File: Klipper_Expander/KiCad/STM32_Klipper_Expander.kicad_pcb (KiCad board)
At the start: 2 copper layers, 100 x 24 mm, 47 parts, among them J1 USB_B_Micro, J10 Conn_01x01, J11 Conn_01x03, J12 Conn_01x02, J2 Conn_01x04, J4 Conn_01x03, J5 Vin, J6 Screw_Terminal_01x08, J7 Conn_01x02, J8 Conn_01x02, J9 Conn_01x02, Q1 IRLML6344TRPBF, Q2 IRLML6344TRPBF, Q3 IRLML6344TRPBF, Q4 IRLML6344TRPBF, SW2 SW_SPST, U1 STM32F042F6Px, U2 AP2127K-3.3, U3 74LVC1G17

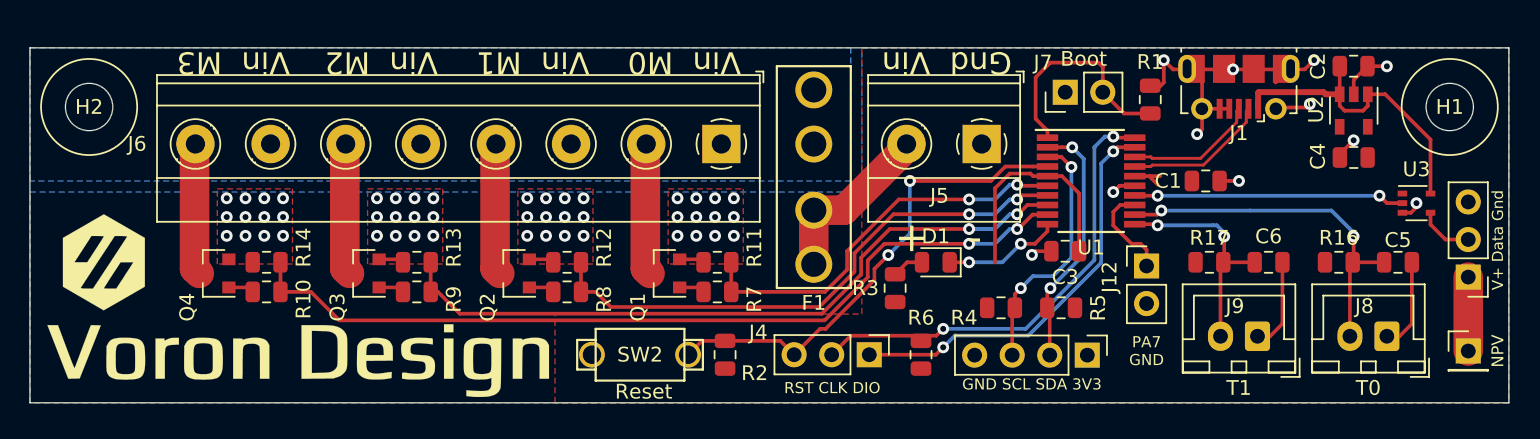
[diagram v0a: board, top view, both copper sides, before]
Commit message: Status LED's and silkscren adjustments.
Added status LED's for Vin (12/24V), USB (5V), and all 4 mosfets on the drain. LED's will signal mosfet output status.

Gerber and PNP files still need to be completed.
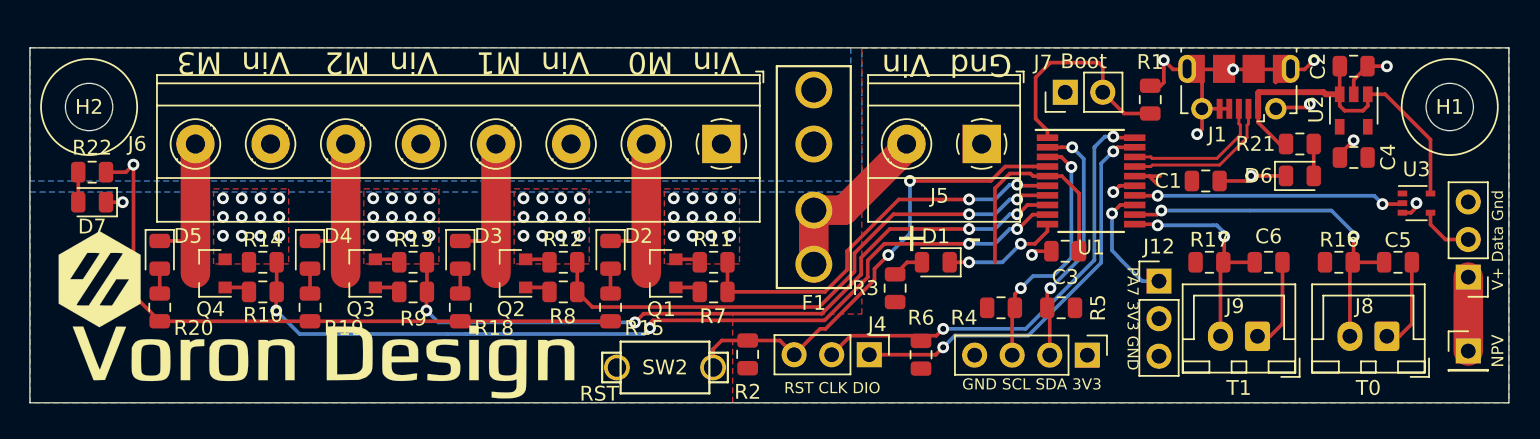
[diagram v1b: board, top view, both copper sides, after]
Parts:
- added D2: LED, LED_SMD:LED_0805_2012Metric, F.Cu at (139.3, 90.0)
- added D3: LED, LED_SMD:LED_0805_2012Metric, F.Cu at (129.1, 90.0)
- added D4: LED, LED_SMD:LED_0805_2012Metric, F.Cu at (118.9, 90.0)
- added D5: LED, LED_SMD:LED_0805_2012Metric, F.Cu at (108.8, 90.0)
- added D6: LED, LED_SMD:LED_0805_2012Metric, F.Cu at (185.9, 84.7)
- added D7: LED, LED_SMD:LED_0805_2012Metric, F.Cu at (104.2, 86.4)
- added R15: 4.7K, Resistor_SMD:R_0805_2012Metric, F.Cu at (139.3, 93.5)
- added R18: 4.7K, Resistor_SMD:R_0805_2012Metric, F.Cu at (129.1, 93.5)
- added R19: 4.7K, Resistor_SMD:R_0805_2012Metric, F.Cu at (118.9, 93.5)
- added R20: 4.7K, Resistor_SMD:R_0805_2012Metric, F.Cu at (108.8, 93.5)
- added R21: 1K, Resistor_SMD:R_0805_2012Metric, F.Cu at (185.9, 82.5)
- added R22: 4.7K, Resistor_SMD:R_0805_2012Metric, F.Cu at (104.2, 84.4)
- J12: value Conn_01x02 -> Conn_01x03; footprint Connector_PinHeader_2.54mm:PinHeader_1x02_P2.54mm_Vertical -> Connector_PinHeader_2.54mm:PinHeader_1x03_P2.54mm_Vertical
- moved SW2 1.90 mm to (142.9, 97.6)
- moved G*** 1.71 mm to (120.0, 96.6)
- moved R2 1.53 mm to (148.5, 96.7)
- moved J12 1.32 mm to (176.3, 91.8)
- moved G*** 1.18 mm to (104.7, 91.6)
- moved Q1 0.25 mm to (142.7, 91.2)
- moved Q2 0.25 mm to (132.5, 91.2)
- moved Q3 0.25 mm to (122.4, 91.2)
- moved Q4 0.25 mm to (112.2, 91.2)
- moved R10 0.25 mm to (115.7, 92.5)
- moved R14 0.25 mm to (115.7, 90.5), turned to 180 degrees
- moved R11 0.25 mm to (146.2, 90.5), turned to 180 degrees
- moved R12 0.25 mm to (136.1, 90.5), turned to 180 degrees
- moved R13 0.25 mm to (125.9, 90.5), turned to 180 degrees
- moved R7 0.25 mm to (146.2, 92.5)
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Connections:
- J12 pad 2: GND -> +3V3
- R11 pad 1: GND -> PWM0
- R11 pad 2: PWM0 -> GND
- R12 pad 1: GND -> PWM1
- R12 pad 2: PWM1 -> GND
- R13 pad 1: GND -> PWM2
- R13 pad 2: PWM2 -> GND
- R14 pad 1: GND -> PWM3
- R14 pad 2: PWM3 -> GND
- R16 pad 1: +3V3 -> T0
- R16 pad 2: T0 -> +3V3
- R17 pad 1: +3V3 -> T1
- R17 pad 2: T1 -> +3V3
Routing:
- net /Vin: track 0.00 -> 43.9 mm, vias 0 -> 1
- net GND: track 52.3 -> 56.7 mm, vias 59 -> 60
- net VCC: track 21.5 -> 24.8 mm
- net Net-(D6-Pad2): track 0.00 -> 2.16 mm
- net /Mosfet0: track 9.02 -> 11.2 mm
- net /Mosfet2: track 9.02 -> 11.2 mm
- net /Mosfet3: track 9.02 -> 11.2 mm
- net /Mosfet1: track 9.02 -> 11.2 mm
- net Net-(D7-Pad2): track 0.00 -> 2.03 mm
- net PWM3: track 58.3 -> 60.3 mm, vias 2 -> 4
- net GPIO: track 6.59 -> 8.33 mm, vias 0 -> 1
- net Net-(D5-Pad2): track 0.00 -> 1.68 mm
- net Net-(D4-Pad2): track 0.00 -> 1.68 mm
- net Net-(D3-Pad2): track 0.00 -> 1.68 mm
- net Net-(D2-Pad2): track 0.00 -> 1.68 mm
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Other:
- board text added: "PA7 3V3 GND"
- board text added: "RST"
- board text removed: "PA7 GND"
- board text removed: "Reset"

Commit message: Updated Gerber and Production files, Minor changes
Changed thermsitor pullups to 4K7 to increse range and reliability.
Added silkscreen to indicate what the status LED's are showing.
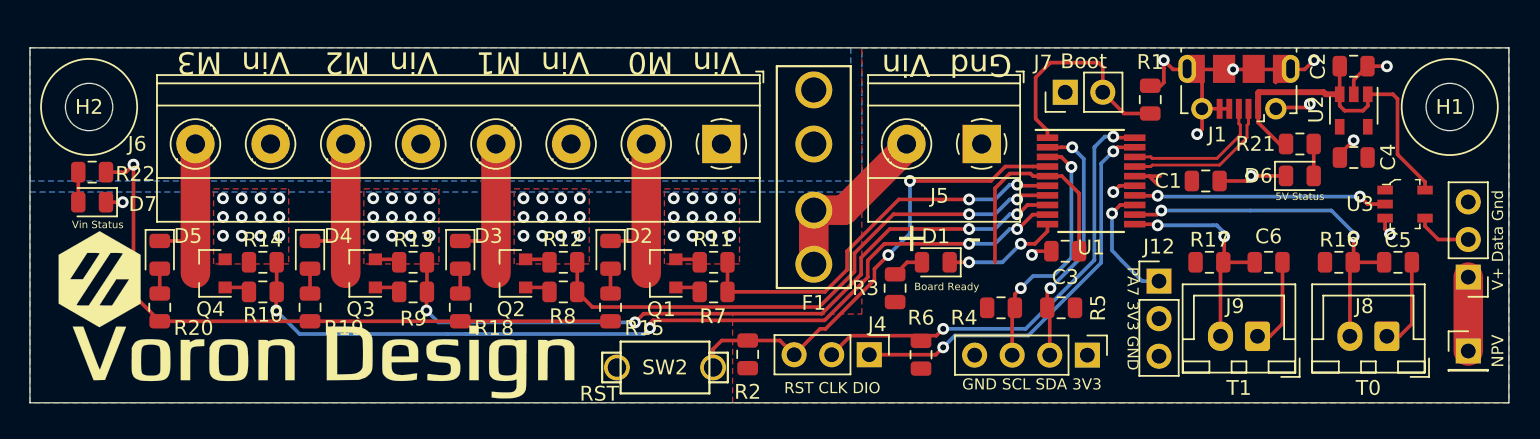
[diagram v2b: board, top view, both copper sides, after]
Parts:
- R16, R17: value 10K -> 4.7K
- U3: footprint Package_TO_SOT_SMD:SOT-353_SC-70-5 -> digikey-footprints:SOT-753
- moved U3 0.77 mm to (193.0, 86.6), turned to 270 degrees
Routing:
- net Neopixel: track 18.4 -> 17.2 mm
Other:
- board text added: "5V Status"
- board text added: "Board Ready"
- board text added: "Vin Status"

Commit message: Change from global to Project based library
Project based libraary added which includes all schematic symbols, footprints, and 3D models
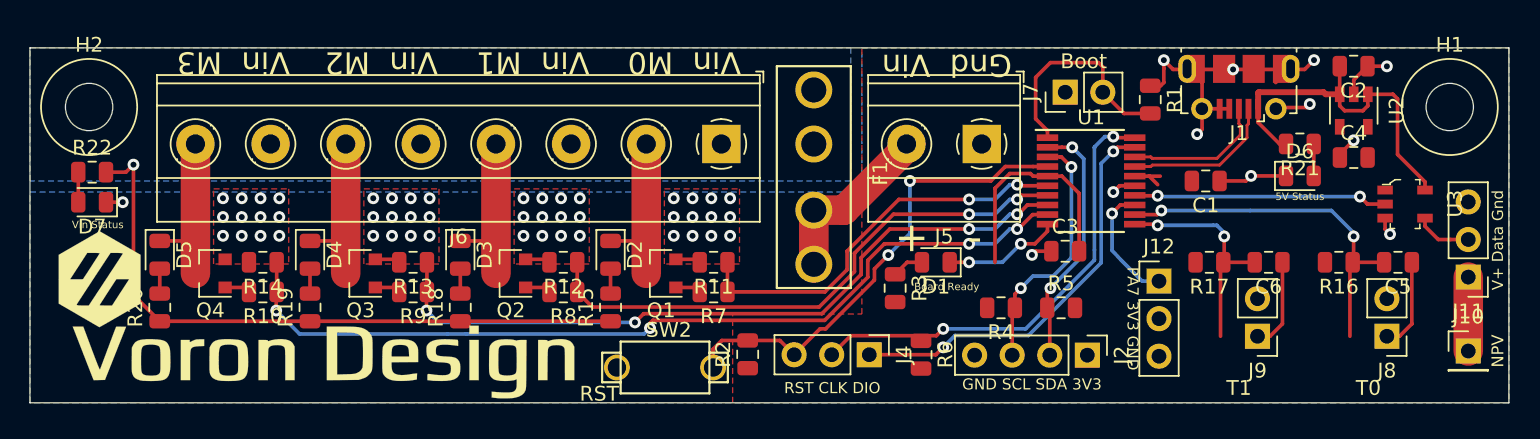
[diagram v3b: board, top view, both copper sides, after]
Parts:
- C1, C2, C3, C4, C5, C6: footprint Capacitor_SMD:C_0805_2012Metric -> KlipperExpander:C_0805_2012Metric
- D1, D2, D3, D4, D5, D6, D7: footprint LED_SMD:LED_0805_2012Metric -> KlipperExpander:LED_0805_2012Metric
- F1: footprint TRA_KiCad_Footprints:3544-2_FuseHolder -> KlipperExpander:3544-2_FuseHolder
- H1, H2: footprint MountingHole:MountingHole_3.2mm_M3 -> KlipperExpander:MountingHole_3.2mm_M3
- J1: footprint TRA_KiCad_Footprints:Molex-105017-0001-USBMicroB -> KlipperExpander:Molex-105017-0001-USBMicroB
- J10: footprint Connector_PinHeader_2.54mm:PinHeader_1x01_P2.54mm_Vertical -> KlipperExpander:PinHeader_1x01_P2.54mm_Vertical
- J11, J12, J4: footprint Connector_PinHeader_2.54mm:PinHeader_1x03_P2.54mm_Vertical -> KlipperExpander:PinHeader_1x03_P2.54mm_Vertical
- J2: footprint Connector_PinHeader_2.54mm:PinHeader_1x04_P2.54mm_Vertical -> KlipperExpander:PinHeader_1x04_P2.54mm_Vertical
- J5: footprint TRA_KiCad_Footprints:1x02_ScrewTerminal_Phoenix -> KlipperExpander:1x02_ScrewTerminal_Phoenix
- J6: footprint TRA_KiCad_Footprints:TerminalBlock_Phoenix_MKDS-1,5-8-5.08_1x08_P5.08mm_Horizontal -> KlipperExpander:1x08_ScrewTerminal_Phoenix
- J7: footprint Connector_PinHeader_2.54mm:PinHeader_1x02_P2.54mm_Vertical -> KlipperExpander:PinHeader_1x02_P2.54mm_Vertical
- J8, J9: footprint Connector_JST:JST_XH_B02B-XH-A_1x02_P2.50mm_Vertical -> KlipperExpander:PinHeader_1x02_P2.54mm_Vertical
- Q1, Q2, Q3, Q4: footprint Package_TO_SOT_SMD:SOT-23 -> KlipperExpander:SOT-23
- R1, R10, R11, R12, R13, R14, R15, R16, R17, R18, R19, R2, R20, R21, R22, R3, R4, R5, R6, R7, R8, R9: footprint Resistor_SMD:R_0805_2012Metric -> KlipperExpander:R_0805_2012Metric
- SW2: footprint TRA_KiCad_Footprints:2PinTactileButton -> KlipperExpander:2PinTactileButton
- U1: footprint Package_SO:TSSOP-20_4.4x6.5mm_P0.65mm -> KlipperExpander:TSSOP-20_4.4x6.5mm_P0.65mm
- U2: footprint Package_TO_SOT_SMD:SOT-23-5 -> KlipperExpander:SOT-23-5
- U3: footprint digikey-footprints:SOT-753 -> KlipperExpander:SOT-753

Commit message: Silkscreen adjustment and capacitro simplifications
Changed C5 and C6 from 10uF to 4.7uF for part simplification.

Change silkscreen sizings for better printing
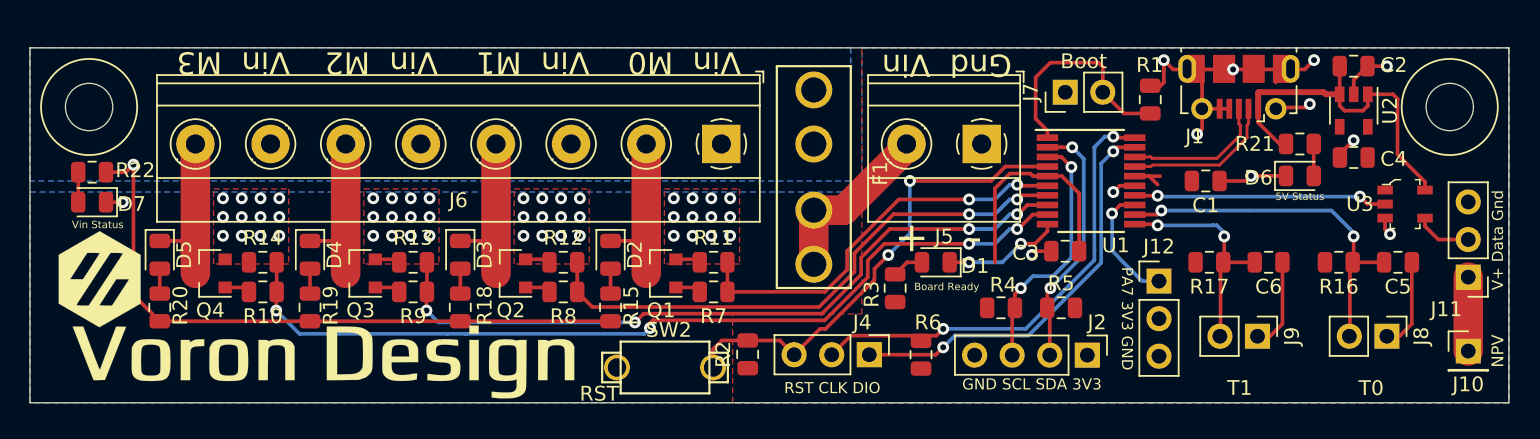
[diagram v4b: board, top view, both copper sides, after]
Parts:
- C5, C6: value 10uF -> 4.7uF
- turned J8 to 270 degrees
- turned J9 to 270 degrees
